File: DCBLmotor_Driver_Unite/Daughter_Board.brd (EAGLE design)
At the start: 104.2 x 72.3 mm, 72 parts, among them CN1 DF11-16DP-2DSA, CN2 26-01-3115, CN3 39-28-1023, IC1 ACS780KLRTR-150B-T, IC2 IR2010SPBF, IC3 IR2010SPBF, IC4 IR2010SPBF, IC5 ACS780KLRTR-150B-T, IC6 ACS780KLRTR-150B-T

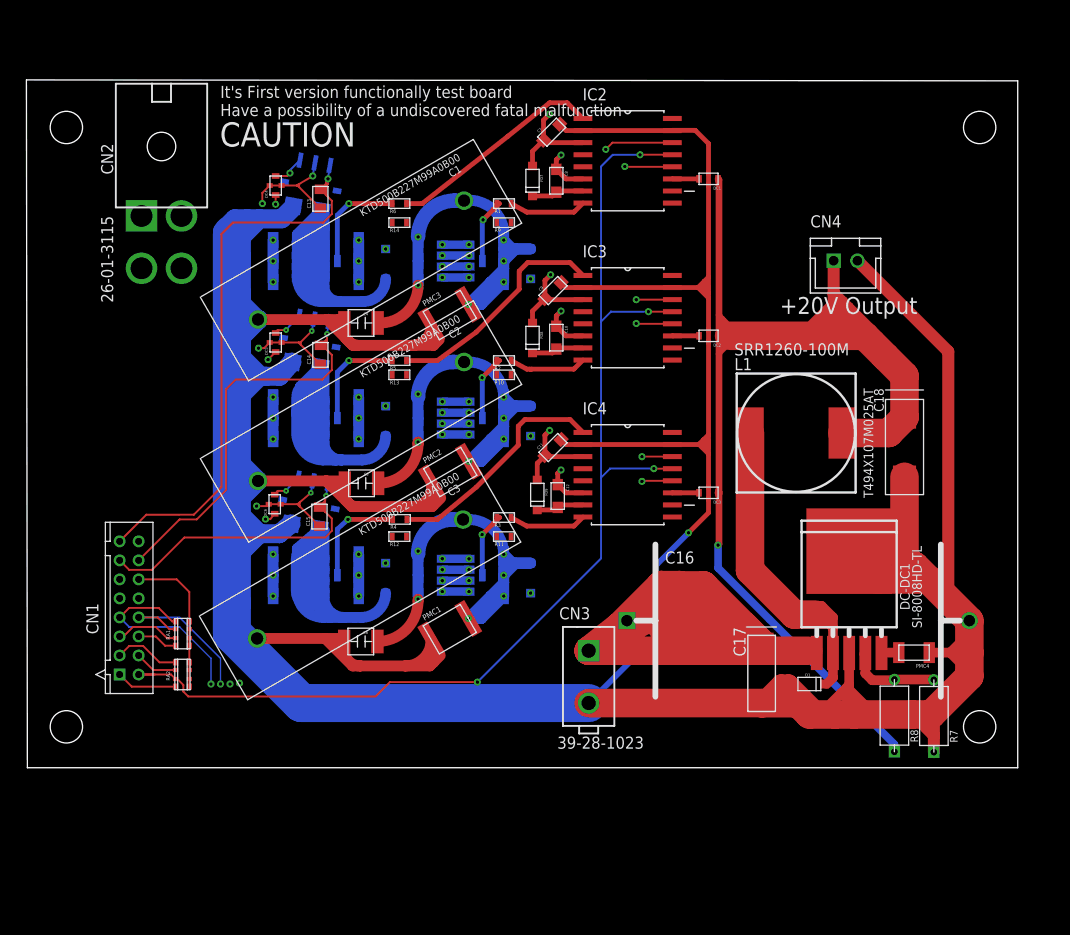
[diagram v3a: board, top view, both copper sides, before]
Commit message: Resister for Quartz crystalstal
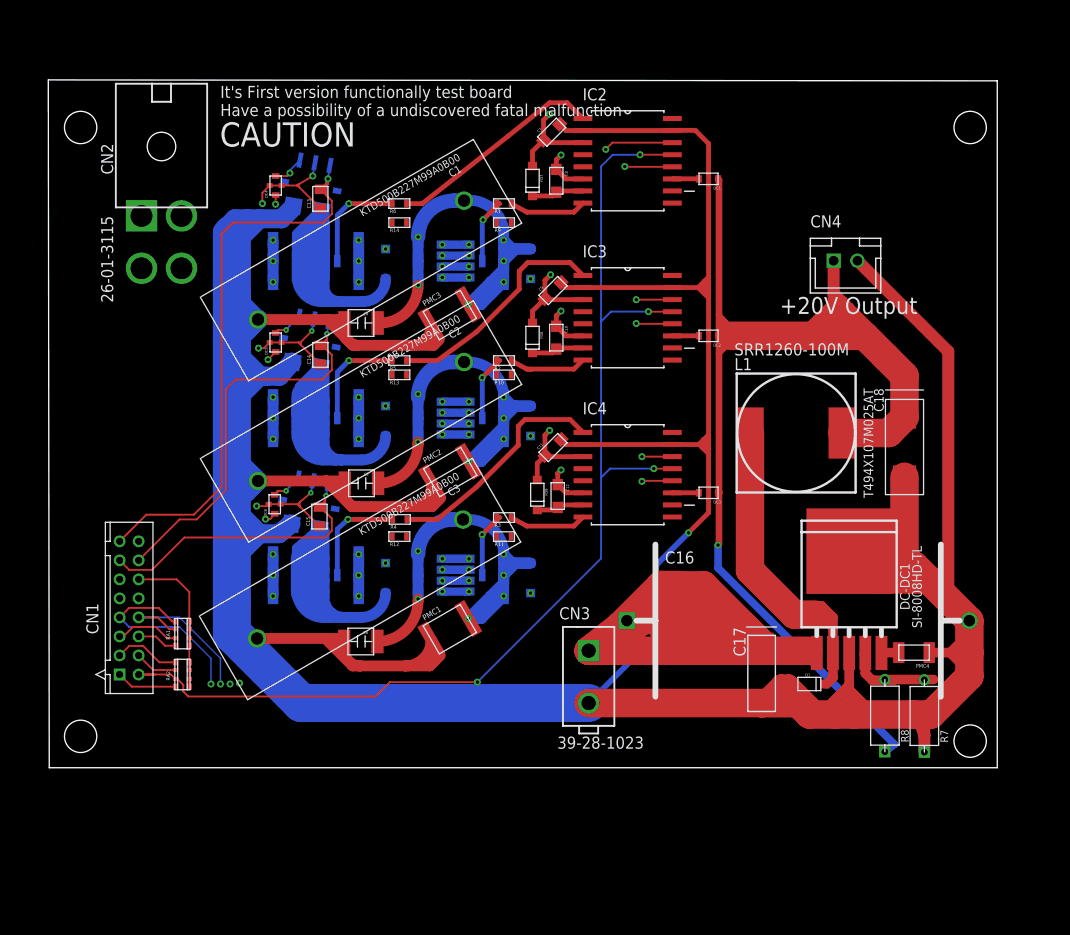
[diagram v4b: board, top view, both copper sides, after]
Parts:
- moved R7 1.00 mm to (92.2, 13.1)
- moved R8 1.00 mm to (88.0, 13.2)
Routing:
- net N$17: track 11.0 -> 13.8 mm
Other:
- board size 104.2 x 72.3 mm -> 99.8 x 72.3 mm
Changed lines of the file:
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@@
 <setting verticaltext="up"/>
 </settings>
-<grid distance="0.01" unitdist="mm" unit="mm" style="lines" multiple="1" display="no" altdistance="5" altunitdist="mil" altunit="mm"/>
+<grid distance="0.5" unitdist="mm" unit="mm" style="lines" multiple="1" display="no" altdistance="5" altunitdist="mil" altunit="mm"/>
 <layers>
 <layer number="1" name="Top" color="4" fill="1" visible="yes" active="yes"/>
@@
 <board>
 <plain>
-<wire x1="-2.1" y1="7.7" x2="102" y2="7.7" width="0" layer="20"/>
-<wire x1="102" y1="7.7" x2="102" y2="79.9" width="0" layer="20"/>
-<wire x1="102" y1="79.9" x2="-2.2" y2="80" width="0" layer="20"/>
-<wire x1="-2.2" y1="80" x2="-2.1" y2="7.7" width="0" layer="20"/>
+<wire x1="0.2" y1="7.7" x2="99.85" y2="7.7" width="0" layer="20"/>
+<wire x1="99.85" y1="7.7" x2="99.85" y2="79.9" width="0" layer="20"/>
+<wire x1="99.85" y1="79.9" x2="0.1" y2="80" width="0" layer="20"/>
+<wire x1="0.1" y1="80" x2="0.2" y2="7.7" width="0" layer="20"/>
 <text x="77" y="55.4" size="1.778" layer="21">+20V Output</text>
 <text x="52.525" y="12.2" size="1.27" layer="22" rot="MR0">It's First version functionally test board
@@
 Have a possibility of a undiscovered fatal malfunction</text>
 <text x="18.125" y="73" size="2.54" layer="21">CAUTION</text>
-<hole x="2" y="12" drill="3.4"/>
-<hole x="2" y="75" drill="3.4"/>
-<hole x="98" y="75" drill="3.4"/>
-<hole x="98" y="12" drill="3.4"/>
+<hole x="3.5" y="11" drill="3.4"/>
+<hole x="3.5" y="75" drill="3.4"/>
+<hole x="97" y="75" drill="3.4"/>
+<hole x="97" y="10.5" drill="3.4"/>
 </plain>
 <attributes>
@@
 <element name="C18" library="KEMET" package="T494_X" value="T494X107M025AT" x="90.099634375" y="41.411209375" rot="R270"/>
 <element name="L1" library="Bourns" package="SRR1260" value="SRR1260-100M" x="78.70994375" y="42.88495625"/>
-<element name="R7" library="VISHAY" package="CMF55" value="RN55C8000BB14" x="93.18589375" y="13.140809375" rot="R90"/>
-<element name="R8" library="VISHAY" package="CMF55" value="RN55C1912BB14" x="89.036859375" y="13.17445625" rot="R90"/>
+<element name="R7" library="VISHAY" package="CMF55" value="RN55C8000BB14" x="92.18589375" y="13.140809375" rot="R90"/>
+<element name="R8" library="VISHAY" package="CMF55" value="RN55C1912BB14" x="88.036859375" y="13.17445625" rot="R90"/>
 <element name="D1" library="DIODE" package="SOD123" value="1N5711W-7-F" x="81.7" y="16.5" rot="R180"/>
 <element name="PMC4" library="Rubycon" package="3216" value="50ST104MA13216" x="89.5" y="19.8"/>
@@
 <contactref element="IC4" pad="2"/>
 <contactref element="C11" pad="P$1"/>
-<wire x1="56.301" y1="41.675" x2="56.02" y2="41.675" width="0.508" layer="1"/>
-<wire x1="56.02" y1="41.675" x2="54.532109375" y2="41.675" width="0.508" layer="1"/>
+<wire x1="56.301" y1="41.675" x2="54.532109375" y2="41.675" width="0.508" layer="1"/>
 <wire x1="54.532109375" y1="41.675" x2="54" y2="42.207109375" width="0.508" layer="1"/>
-<wire x1="93.18589375" y1="9.340809375" x2="93.18589375" y2="11.1" width="1.27" layer="1"/>
-<wire x1="93.18589375" y1="11.1" x2="93.18589375" y2="13.01410625" width="1.27" layer="1"/>
-<wire x1="93.18589375" y1="13.01410625" x2="92.9" y2="13.3" width="1.27" layer="1"/>
-<wire x1="93.18589375" y1="11.1" x2="91.68589375" y2="12.6" width="1.27" layer="1"/>
+<wire x1="92.18589375" y1="9.340809375" x2="92.18589375" y2="11.1" width="1.27" layer="1"/>
+<wire x1="92.18589375" y1="11.1" x2="92.18589375" y2="13.01410625" width="1.27" layer="1"/>
+<wire x1="92.18589375" y1="13.01410625" x2="92.9" y2="13.3" width="1.27" layer="1"/>
+<wire x1="92.18589375" y1="11.1" x2="91.68589375" y2="12.6" width="1.27" layer="1"/>
 <wire x1="91.68589375" y1="12.6" x2="91.5" y2="12.6" width="1.27" layer="1"/>
 <wire x1="91.5" y1="12.6" x2="91.5" y2="12.7" width="1.27" layer="1"/>
@@
 <wire x1="56.301" y1="73.405" x2="52.40799375" y2="73.405" width="0.508" layer="1"/>
 <wire x1="52.40799375" y1="73.405" x2="52.156496875" y2="73.656496875" width="0.508" layer="1"/>
-<wire x1="89.036859375" y1="9.37445625" x2="89.036859375" y2="10.163140625" width="0.8128" layer="16"/>
+<wire x1="88.036859375" y1="9.37445625" x2="89.036859375" y2="10.163140625" width="0.8128" layer="16"/>
 <wire x1="89.036859375" y1="10.163140625" x2="75.9" y2="23.3" width="0.8128" layer="16"/>
 <wire x1="52.302940625" y1="57.01005" x2="52.302940625" y2="58.922940625" width="0.508" layer="1"/>
@@
 <wire x1="85.979053125" y1="19.766625" x2="85.909875" y2="18.622334375" width="0.8128" layer="1"/>
 <wire x1="85.840809375" y1="19.62838125" x2="85.979053125" y2="19.766625" width="1" layer="1"/>
-<wire x1="93.152246875" y1="16.97445625" x2="93.18589375" y2="16.940809375" width="0.6096" layer="1"/>
+<wire x1="93.152246875" y1="16.97445625" x2="92.18589375" y2="16.940809375" width="0.6096" layer="1"/>
 <wire x1="85.979053125" y1="19.766625" x2="85.979053125" y2="17.620946875" width="1.016" layer="1"/>
 <wire x1="85.979053125" y1="17.620946875" x2="86.7" y2="16.9" width="1.016" layer="1"/>
 <wire x1="86.7" y1="16.9" x2="88.962403125" y2="16.9" width="1.016" layer="1"/>
-<wire x1="88.962403125" y1="16.9" x2="89.036859375" y2="16.97445625" width="1.016" layer="1"/>
-<wire x1="89.036859375" y1="16.97445625" x2="93.152246875" y2="16.97445625" width="1.016" layer="1"/>
+<wire x1="88.962403125" y1="16.9" x2="88.036859375" y2="16.97445625" width="1.016" layer="1"/>
+<wire x1="88.036859375" y1="16.97445625" x2="93.152246875" y2="16.97445625" width="1.016" layer="1"/>
 </signal>
 <signal name="N$31">

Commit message: Change Driver borard
Change FETs and Gatedriver
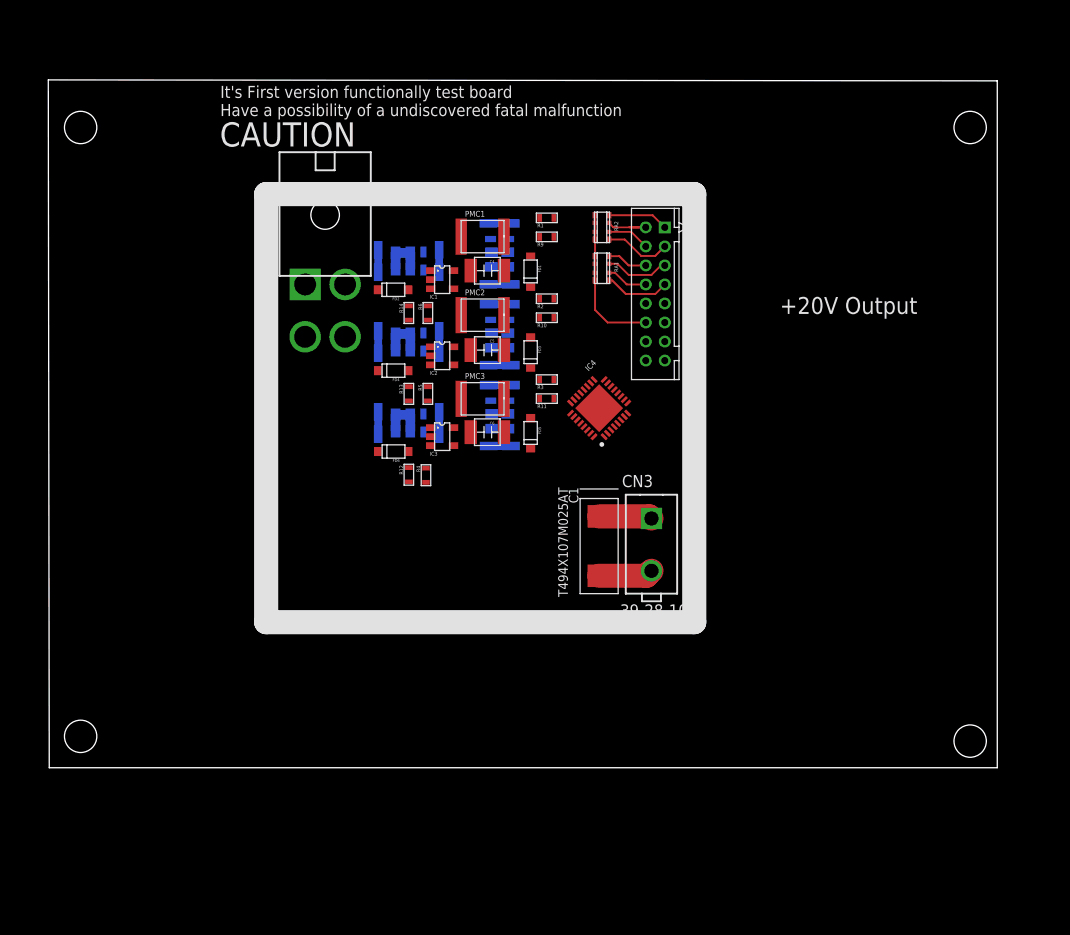
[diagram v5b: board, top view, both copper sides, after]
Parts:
- removed C10, C11, C12, C7, C8, C9: C2012JB0J476M125AC, TDK:C2012
- removed C13, C14, C15: CGA1A2C0G1E180J030BA, TDK:CC0603
- removed C16: MAL202117152E3, VISHAY:012AMS13*30
- removed C17: T495D475K050ATE275, KEMET:T495_D
- removed C18: T494X107M025AT, KEMET:T494_X
- removed C2, C3: KTD500B227M99A0B00, United_Chemi-con:TKA50V_150U-220
- removed CN4: (no value), jst-xh:B2B-XH-A
- removed D1: 1N5711W-7-F, DIODE:SOD123
- removed DC-DC1: SI-8008HD-TL, SANKEN:D2_PACAGE_5PIN
- removed DC1, DC2, DC3, DC4, DC5, DC6: YFF21PC1E104MT000N, TDK:YFF21PC
- removed FD7, FD8, FD9: 1N4448WQ-7-F, DIODE:SOD123
- removed IC5, IC6: ACS780KLRTR-150B-T, ACS780:7-PIN_PSOP
- removed L1: SRR1260-100M, Bourns:SRR1260
- removed PMC4: 50ST104MA13216, Rubycon:3216
- removed R7: RN55C8000BB14, VISHAY:CMF55
- removed R8: RN55C1912BB14, VISHAY:CMF55
- C1: value KTD500B227M99A0B00 -> T494X107M025AT; device United_Chemi-con:TKA50V_150U-220 -> KEMET:T494_X
- FET1, FET2, FET3, FET4, FET5, FET6: value IRF7739L1TRPBF -> IRF7480MTRPBF; device Infinion:DIRECT_FET-L8 -> Infinion:DIRECT_FET_ME
- IC1: value ACS780KLRTR-150B-T -> IR25750LPBF; device ACS780:7-PIN_PSOP -> Infinion:SOT-23-L5
- IC2, IC3: value IR2010SPBF -> IR25750LPBF; device IR2010SPBF:SOIC127P1032X265-16N -> Infinion:SOT-23-L5
- IC4: value IR2010SPBF -> DRV8320SRTVT; device IR2010SPBF:SOIC127P1032X265-16N -> DRV8320SRTVT:QFN50P500X500X80-33N
- moved CN1 74.1 mm to (64.9, 64.5), turned to 90 degrees
- moved RA2 64.5 mm to (58.3, 64.5), turned to 270 degrees
- moved RA1 58.5 mm to (58.3, 60.2), turned to 270 degrees
- moved PMC1 40.3 mm to (48.0, 63.5), turned to 180 degrees
- moved C1 39.0 mm to (58.0, 31.0), turned to 270 degrees
- moved IC2 28.3 mm to (41.5, 51.0), turned to 270 degrees
- moved C6 25.7 mm to (48.0, 43.0)
- moved IC3 23.2 mm to (41.5, 42.5), turned to 270 degrees
- moved C5 19.3 mm to (48.0, 51.6)
- moved CN2 18.6 mm to (29.2, 58.5)
- moved FET6 17.7 mm to (38.0, 43.9)
- moved IC1 16.9 mm to (41.5, 59.0), flipped to the top, turned to 270 degrees
- moved FET5 16.9 mm to (47.6, 44.7), turned to 270 degrees
- moved PMC2 15.8 mm to (48.0, 55.3), turned to 180 degrees
- moved CN3 15.4 mm to (63.5, 33.9)
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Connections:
- removed net +20V: C11.P$2, C18.P$+, C7.P$2, C9.P$2, CN4.1, DC1.P$2, DC2.P$2, DC3.P$2, FD7.A, FD8.A, FD9.A, IC2.3, IC3.3, IC4.3, L1.P$2, R8.P$1
- removed net N$10: DC5.P$1, IC5.P$1
- removed net N$14: FET4.G, R13.P$1, R5.P$1
- removed net N$15: FD6.A, FET6.S1, FET6.S2, FET6.S3, FET6.S4, FET6.S5, FET6.S6, FET6.S7, FET6.S8, IC6.P$5, R12.P$2
- removed net N$16: DC6.P$1, IC6.P$1
- removed net N$17: DC-DC1.P$5, R7.P$2, R8.P$2
- removed net N$23: C8.P$1, FD7.K, IC2.7
- removed net N$25: C10.P$1, FD8.K, IC3.7
- removed net N$27: C12.P$1, FD9.K, IC4.7
- removed net N$28: DC2.P$1, IC3.11
- removed net N$29: DC3.P$1, IC4.11
- removed net N$3: FD2.A, FET2.S1, FET2.S2, FET2.S3, FET2.S4, FET2.S5, FET2.S6, FET2.S7, FET2.S8, IC1.P$5, R14.P$2
- removed net N$30: DC1.P$1, IC2.11
- removed net N$31: DC-DC1.P$6, PMC4.P$1
- removed net N$5: FD4.A, FET4.S1, FET4.S2, FET4.S3, FET4.S4, FET4.S5, FET4.S6, FET4.S7, FET4.S8, IC5.P$5, R13.P$2
- removed net N$7: DC4.P$1, IC1.P$1
- removed net N$8: D1.K, DC-DC1.P$3, L1.P$1
- removed net N$9: FET2.G, R14.P$1, R6.P$1
- new net N$2: FET4.G1, FET4.G2, IC2.P$3, R13.P$2, R5.P$1
- new net N$4: FET2.G1, FET2.G2, R6.P$1
- new net N$6: IC1.P$3, R14.P$2
- net +5V: no longer DC4.P$2, DC5.P$2, DC6.P$2
- net CU1: no longer C13.P$1, IC1.P$3
- net CU2: no longer C14.P$1, IC5.P$3
- net CU3: no longer C15.P$1, IC6.P$3
- net GND: now also FD2.A, FD4.A, FD6.A, FET2.S1, FET2.S2, FET2.S3, FET2.S4, FET4.S1, FET4.S2, FET4.S3, FET4.S4, FET6.S1, FET6.S2, FET6.S3, FET6.S4, IC2.P$4, IC3.P$4, R12.P$1, R13.P$1; no longer C11.P$1, C16.P$2, C17.P$2, C18.P$2, C2.P$2, C3.P$2, C7.P$1, C9.P$1, CN4.2, D1.A, DC-DC1.P$1, DC-DC1.P$4, DC1.GND1, DC1.GND2, DC2.GND1, DC2.GND2, DC3.GND1, DC3.GND2, IC1.P$6, IC2.15, IC2.2, IC3.15, IC3.2, IC4.15, IC4.2, IC5.P$6, IC6.P$6, PMC4.P$2, R7.P$1
- net GND_LG: no longer C13.P$2, C14.P$2, C15.P$2, DC4.GND1, DC4.GND2, DC5.GND1, DC5.GND2, DC6.GND1, DC6.GND2, IC1.P$2, IC5.P$2, IC6.P$2
- net HIN1: no longer IC2.12
- net HIN2: no longer IC3.12
- net HIN3: no longer IC4.12
- net HO1: no longer IC2.8
- net HO2: no longer IC3.8
- net HO3: no longer IC4.8
- net LIN1: no longer IC2.14
- net LIN2: no longer IC3.14
- net LIN3: no longer IC4.14
- net LO1: no longer IC2.1
- net LO2: no longer IC3.1
- net LO3: no longer IC4.1
- net N$18: now also FET6.G1, FET6.G2, IC3.P$3, R12.P$2; no longer FET6.G, R12.P$1
- net N$19: now also FET5.G1, FET5.G2; no longer FET5.G
- net N$20: now also FET3.G1, FET3.G2; no longer FET3.G
- net N$21: now also FET1.G1, FET1.G2; no longer FET1.G
- net SD: no longer IC2.13, IC3.13, IC4.13
- net VCC: now also C1.P$+, FET1.P$1, FET1.P$2, FET1.P$3, FET1.P$4, FET3.P$1, FET3.P$2, FET3.P$3, FET3.P$4, FET5.P$1, FET5.P$2, FET5.P$3, FET5.P$4; no longer C1.P$1, C16.P$1, C17.P$1, C2.P$1, C3.P$1, DC-DC1.P$2, FET1.D1, FET1.D2, FET1.D3, FET1.D4, FET1.D5, FET1.D6, FET3.D1, FET3.D2, FET3.D3, FET3.D4, FET3.D5, FET3.D6, FET5.D1, FET5.D2, FET5.D3, FET5.D4, FET5.D5, FET5.D6
- net VS1: now also FET2.P$1, FET2.P$2, FET2.P$3, FET2.P$4, IC1.P$5; no longer C8.P$2, FET1.S5, FET1.S6, FET1.S7, FET1.S8, FET2.D1, FET2.D2, FET2.D3, FET2.D4, FET2.D5, FET2.D6, IC2.6
- net VS2: now also FET4.P$1, FET4.P$2, FET4.P$3, FET4.P$4, IC2.P$5; no longer C10.P$2, FET3.S5, FET3.S6, FET3.S7, FET3.S8, FET4.D1, FET4.D2, FET4.D3, FET4.D4, FET4.D5, FET4.D6, IC3.6
- net VS3: now also FET6.P$1, FET6.P$2, FET6.P$3, FET6.P$4, IC3.P$5; no longer C12.P$2, FET5.S5, FET5.S6, FET5.S7, FET5.S8, FET6.D1, FET6.D2, FET6.D3, FET6.D4, FET6.D5, FET6.D6, IC4.6
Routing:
- net GND: track 534.9 -> 20.6 mm, vias 1 -> 0
- net VCC: track 364.9 -> 19.7 mm, vias 18 -> 0
- net +20V: track 169.2 -> 0.00 mm, vias 4 -> 0
- net VS3: track 137.0 -> 4.70 mm, vias 17 -> 0
- net SD: track 122.7 -> 5.77 mm, vias 4 -> 0
- net VS2: track 112.6 -> 4.70 mm, vias 17 -> 0
- net HIN1: track 111.0 -> 7.00 mm, vias 1 -> 0
- net LIN1: track 108.4 -> 4.51 mm, vias 1 -> 0
- net VS1: track 107.7 -> 4.70 mm, vias 17 -> 0
- net GND_LG: track 115.6 -> 15.8 mm, vias 6 -> 0
- net HIN2: track 98.1 -> 6.78 mm, vias 2 -> 0
- net LIN2: track 95.3 -> 4.28 mm, vias 2 -> 0
- net HIN3: track 85.4 -> 6.88 mm, vias 2 -> 0
- net LIN3: track 82.7 -> 4.38 mm, vias 2 -> 0
- net CU1: track 65.8 -> 0.00 mm, vias 1 -> 0
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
